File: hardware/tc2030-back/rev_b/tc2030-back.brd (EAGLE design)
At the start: 5.6 x 8.6 mm, 4 parts

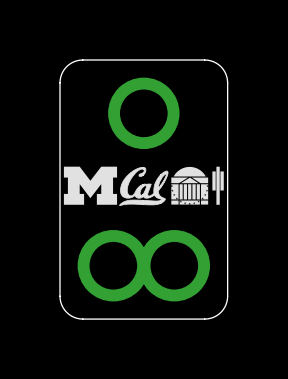
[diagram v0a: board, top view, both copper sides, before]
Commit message: lower logo resolutions for CAM
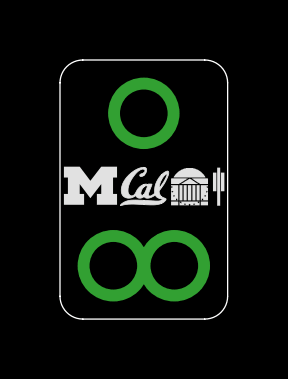
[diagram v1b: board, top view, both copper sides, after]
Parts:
- E$2: device logos:UCSD_TRIDENT_SOLID_50MIL -> logos:UVA_ROTUNDA_50MIL
- E$3: device logos:UVA_ROTUNDA_50MIL -> logos:UCSD_TRIDENT_SOLID_50MIL
- moved E$3 1.42 mm to (5.11, 3.78)
- moved E$2 1.40 mm to (3.68, 3.78)
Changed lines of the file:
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@@
 <setting verticaltext="up"/>
 </settings>
-<grid distance="0.01" unitdist="inch" unit="inch" style="lines" multiple="1" display="yes" altdistance="0.001" altunitdist="inch" altunit="inch"/>
+<grid distance="1" unitdist="mm" unit="mm" style="lines" multiple="1" display="yes" altdistance="0.001" altunitdist="inch" altunit="inch"/>
 <layers>
 <layer number="1" name="Top" color="4" fill="1" visible="yes" active="yes"/>
@@
 <elements>
 <element name="U$2" library="logos" package="UMICH_SOLID_50MIL" value="" x="1.016" y="4.445" smashed="yes"/>
-<element name="E$1" library="logos" package="UCB_CAL_50MIL" value="" x="1.9812" y="3.7846" smashed="yes"/>
-<element name="E$2" library="logos" package="UCSD_TRIDENT_SOLID_50MIL" value="" x="5.08" y="3.81" smashed="yes"/>
-<element name="E$3" library="logos" package="UVA_ROTUNDA_50MIL" value="" x="3.683" y="3.81" smashed="yes"/>
+<element name="E$1" library="logos" package="UCB_CAL_50MIL" value="" x="2.0066" y="3.7846" smashed="yes"/>
+<element name="E$2" library="logos" package="UVA_ROTUNDA_50MIL" value="" x="3.683" y="3.7846" smashed="yes"/>
+<element name="E$3" library="logos" package="UCSD_TRIDENT_SOLID_50MIL" value="" x="5.1054" y="3.7846" smashed="yes"/>
 </elements>
 <signals>
